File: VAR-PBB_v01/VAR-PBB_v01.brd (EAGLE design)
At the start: 78.4 x 86.4 mm, 20 parts, among them J1 ANDERSON_POWER_POLE, J11 CON1X2_SHROUDED, J2 ANDERSON_POWER_POLE, J3 CON1X2_SHROUDED, J4 CON1X2_SHROUDED, J5 CON1X2_SHROUDED, J6 CON1X2_SHROUDED, J7 CON1X2_SHROUDED, J8 CON1X2_SHROUDED, U1 OKI-78SR, U2 XL6009, U3 XL6009, U4 XL6009

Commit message: WIP, but got a ton done.
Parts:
- added C1, C4, C5: 0.1uF, SparkFun-Capacitors:0603
- added C2: 1.0uF, SparkFun-Capacitors:0603
- added C3: 2.2uF, SparkFun-Capacitors:0603
- added R1, R2, R3: (no value), SparkFun-Resistors:0603
- added U5: LP2985AIM5-1.5, LP2985AIM5-1.5:MF05A
- added U6: TPS259271DRCR, TPS259271DRCR:DRC10_1P65X2P40
- moved U$5 91.8 mm to (18.6, 80.0), flipped to the bottom
- moved J5 67.6 mm to (12.7, 33.0), turned to 0 degrees
- moved J3 67.5 mm to (12.7, 22.9), turned to 0 degrees
- moved J4 53.3 mm to (66.0, 73.7), turned to 180 degrees
- moved J8 53.3 mm to (66.0, 63.5), turned to 180 degrees
- moved U3 52.1 mm to (64.9, 35.0)
- moved U4 52.1 mm to (13.6, 34.9)
- moved J9 47.0 mm to (63.5, 2.54), turned to 180 degrees
- moved LOGO1 44.0 mm to (59.1, 82.4), flipped to the bottom
- moved J6 41.9 mm to (12.7, 63.5)
- moved J7 40.6 mm to (12.7, 73.7)
- moved J10 35.6 mm to (20.3, 2.54), turned to 180 degrees
- moved J11 1.80 mm to (66.0, 45.7)
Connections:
- removed net N$6: J10.1
- new net 1.5V_REG: C3.1, J10.1, U5.5
- new net N$12: R3.2, U6.10
- new net N$13: C5.2, U6.2
- new net N$14: R1.1, R2.2, U6.1
- new net N$8: C1.1, U5.4
- net BATT+: now also C2.1, C4.2, U5.1, U5.3, U6.6, U6.7, U6.8
- net GND: now also C1.2, C2.2, C3.2, C4.1, C5.1, R2.1, R3.1, U5.2, U6.11
- net N$1: now also R1.2, U6.3, U6.4, U6.5
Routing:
- net BATT+: track 0.00 -> 158.1 mm, vias 0 -> 3
- net CHANNEL4: track 0.00 -> 79.9 mm, vias 0 -> 1
- net CHANNEL3: track 0.00 -> 71.8 mm
- net 5V_REG: track 0.00 -> 69.8 mm
- net N$11: track 0.00 -> 40.8 mm
- net GND: track 0.00 -> 40.7 mm, vias 0 -> 4
- net N$1: track 0.00 -> 36.7 mm, vias 0 -> 2
- net N$7: track 0.00 -> 18.0 mm
- net N$5: track 0.00 -> 17.5 mm
- net 1.5V_REG: track 0.00 -> 12.6 mm
- net N$3: track 0.00 -> 12.2 mm
- net N$14: track 0.00 -> 4.78 mm
- net N$13: track 0.00 -> 3.99 mm
- net N$12: track 0.00 -> 2.71 mm
- net N$8: track 0.00 -> 2.39 mm
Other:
- board text added: "1.5V Output"
- board text added: "5V Output"
- board text added: "Fix"
- board text added: "Var"

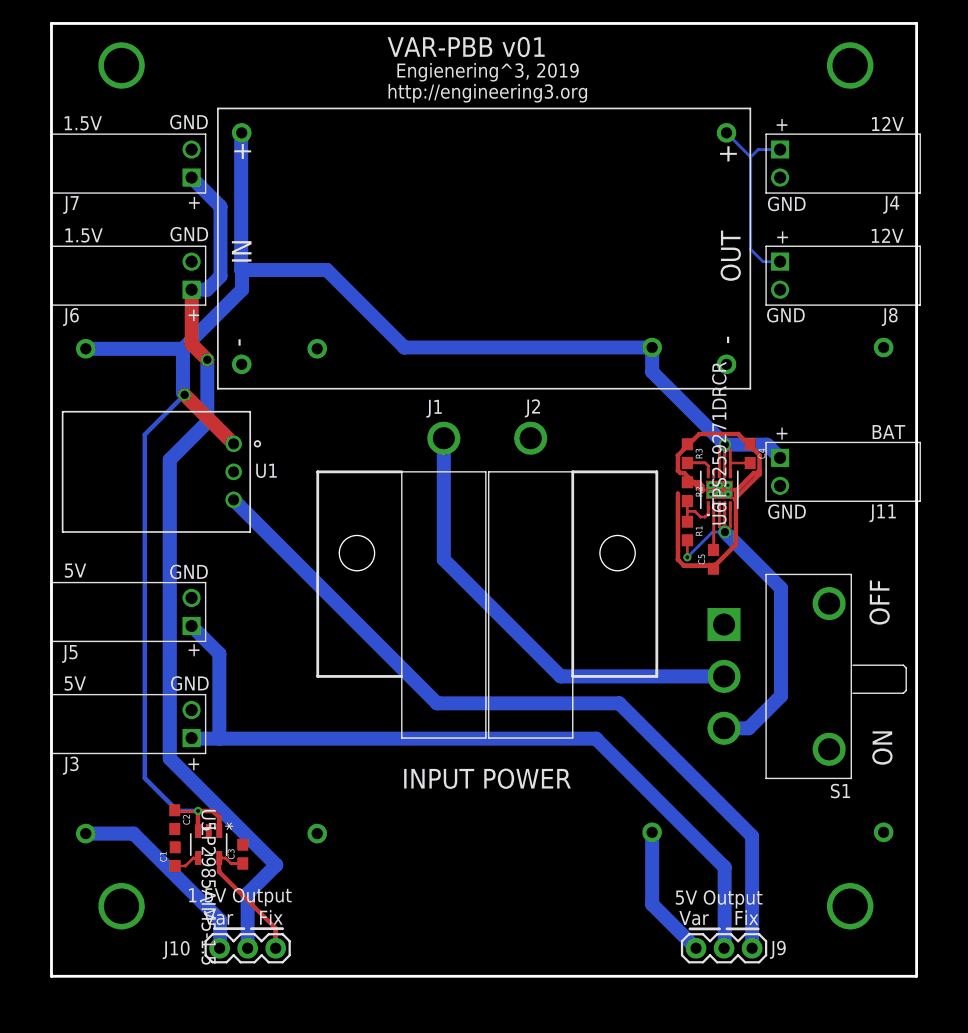
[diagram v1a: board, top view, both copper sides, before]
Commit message: Got all of the features in, board layout done, silk screen tweaked. Need to pick resistor values for UVLO and dV/dT, power LED, and finish BOM xls.
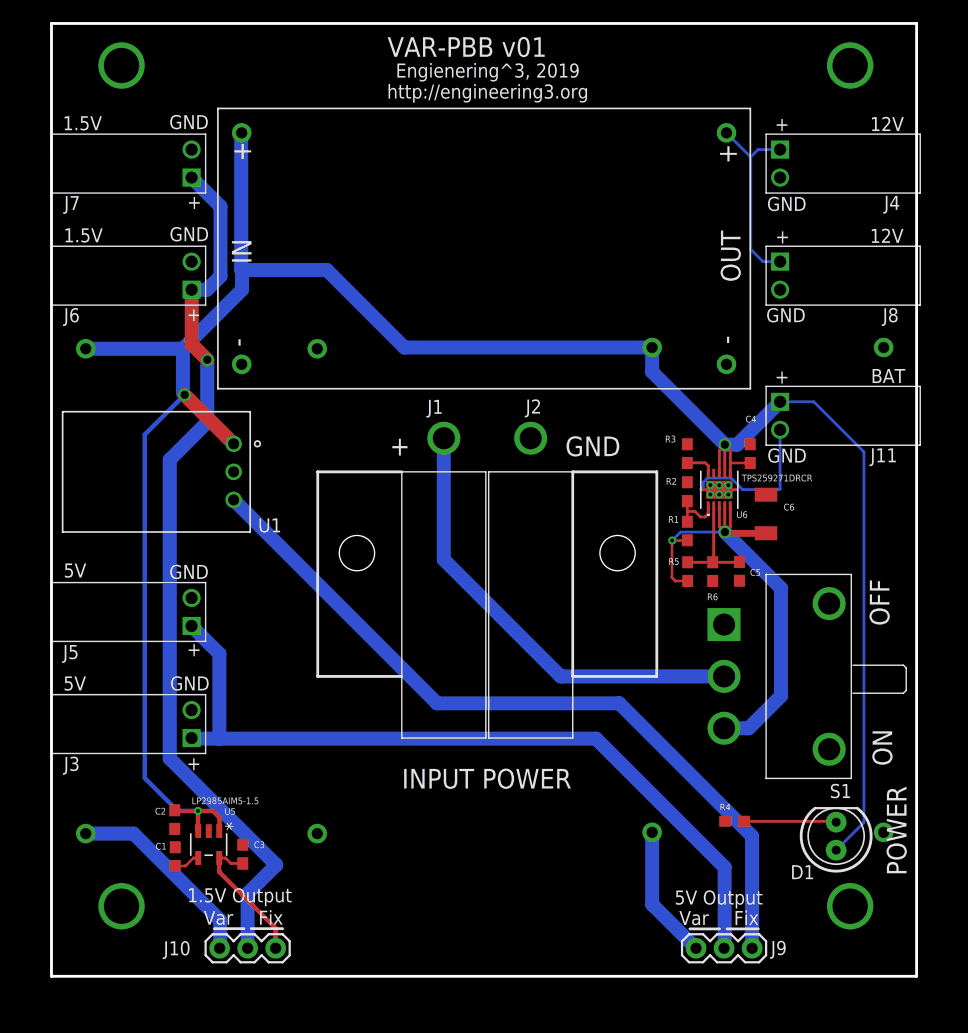
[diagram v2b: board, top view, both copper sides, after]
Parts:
- added C6: 22UF-1210-16V-20%, SparkFun-Capacitors:1210
- added D1: (no value), SparkFun-LED:LED_5MM
- added R4, R5, R6: (no value), SparkFun-Resistors:0603
- moved J11 5.08 mm to (66.0, 50.8)
- moved C5 2.60 mm to (62.4, 36.7)
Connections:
- removed net N$13: C5.2, U6.2
- new net N$2: D1.K, R4.2
- new net N$4: C5.2, R5.1, R6.2, U6.2
- net BATT+: now also D1.A
- net GND: now also C6.2, R4.1, R6.1
- net N$1: now also C6.1, R5.2
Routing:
- net BATT+: track 158.1 -> 205.8 mm
- net GND: track 40.7 -> 17.0 mm, vias 4 -> 10
- net N$4: track 0.00 -> 9.84 mm
- net N$1: track 36.7 -> 46.0 mm
- net N$2: track 0.00 -> 8.38 mm
- net N$13: track 3.99 -> 0.00 mm
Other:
- board text added: "POWER"

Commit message: v01 done - schematic complete and cleaned up, board fully routed, passes DRC, BOM complete.
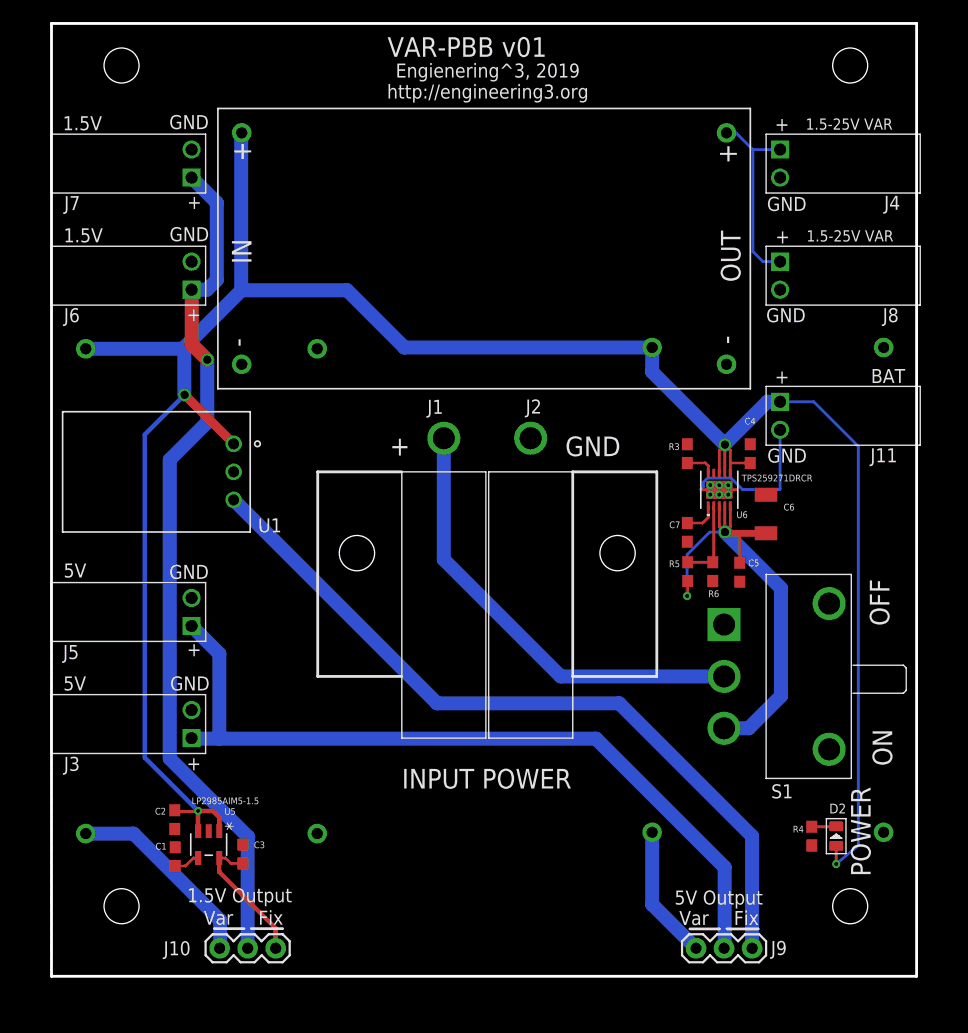
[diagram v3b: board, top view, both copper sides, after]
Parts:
- removed D1: (no value), SparkFun-LED:LED_5MM
- removed LOGO1: OSHW-LOGOM, SparkFun-Aesthetics:OSHW-LOGO-M
- removed R1, R2: (no value), SparkFun-Resistors:0603
- removed U$5: ROHS_GARBAGE, SchmalzHausPublic:ROHS_GARBAGE_5MM
- added C7: DNP, SparkFun-Capacitors:0603
- added D2: RED-0805, OPL_Optoelectronics:LED-0805
- C4, C5: value 0.1uF -> 1uF
- C6: value 22UF-1210-16V-20% -> 22uF
- R3: value (none) -> 45.3K
- R4: value (none) -> 392
- R5: value (none) -> 1M
- R6: value (none) -> 220K
- moved U$6 10.2 mm to (33.3, 3.43)
- moved LOGO2 8.98 mm to (25.7, 5.79)
- moved R4 7.11 mm to (68.9, 12.7), turned to 90 degrees
- moved C5 0.08 mm to (62.4, 36.6)
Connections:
- net BATT+: now also D2.+; no longer D1.A
- net GND: now also C7.1; no longer R2.1
- net N$1: now also C5.2; no longer R1.2
- net N$14: now also C7.2; no longer R1.1, R2.2
- net N$2: now also D2.-; no longer D1.K
- net N$4: no longer C5.2
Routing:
- net N$2: track 8.38 -> 2.23 mm
- net N$4: track 9.84 -> 7.41 mm
- net CHANNEL4: track 79.9 -> 77.5 mm
- net N$14: track 4.78 -> 3.13 mm
- net BATT+: track 205.8 -> 206.6 mm, vias 3 -> 4
- net N$1: track 46.0 -> 46.7 mm
- net GND: track 17.0 -> 16.8 mm, vias 10 -> 6
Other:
- board text added: "1.5-25V VAR"
- board text removed: "12V"

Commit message: Latest version of VAR-PBB, as built. Updated under voltage cutout resistor to get UVLO to around 8.1 V.
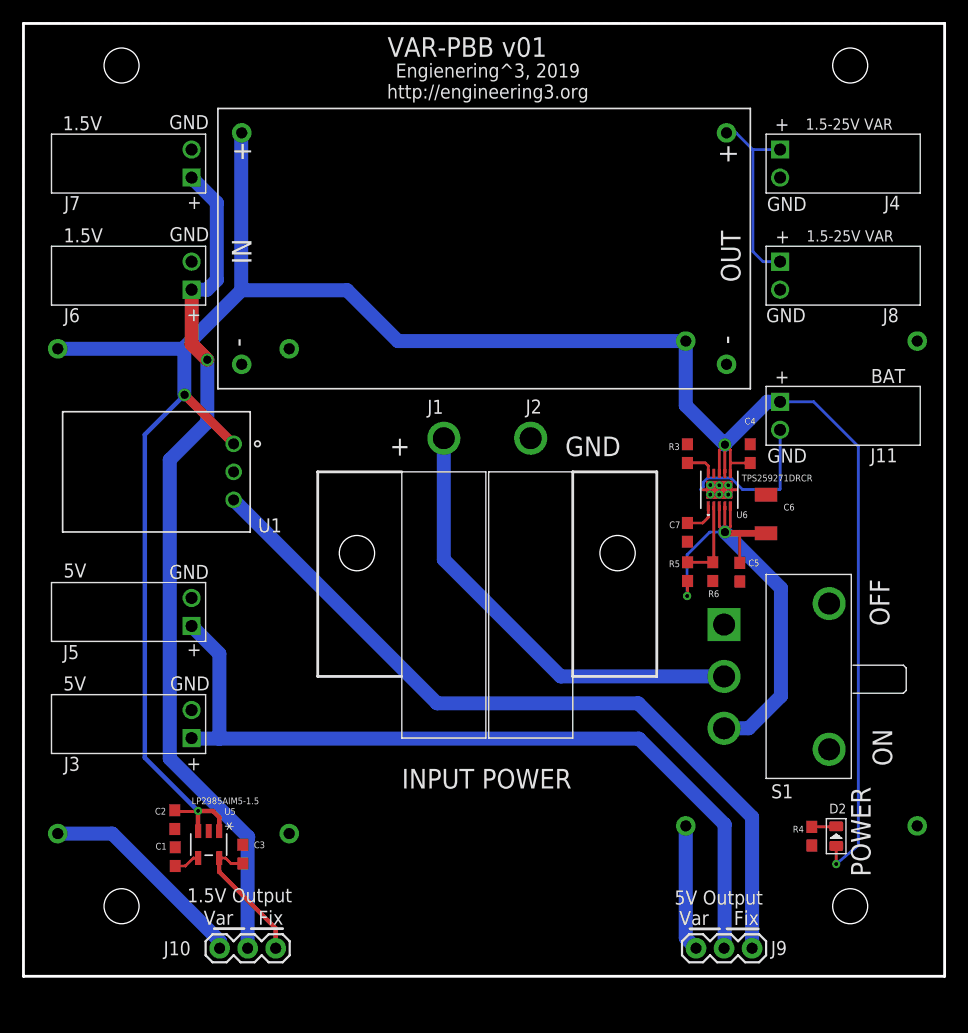
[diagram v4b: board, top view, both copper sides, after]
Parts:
- R6: value 220K -> 213K
- moved U3 3.10 mm to (68.0, 35.6)
- moved U4 2.54 mm to (11.1, 34.9)
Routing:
- net BATT+: track 206.6 -> 211.3 mm
- net CHANNEL3: track 71.8 -> 74.1 mm
- net N$7: track 18.0 -> 19.4 mm
- net 5V_REG: track 69.8 -> 70.8 mm
- net N$3: track 12.2 -> 11.5 mm
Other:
- board size 78.4 x 86.4 mm -> 83.5 x 86.4 mm
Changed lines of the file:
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@@
 <layer number="20" name="Dimension" color="15" fill="1" visible="yes" active="yes"/>
 <layer number="21" name="tPlace" color="7" fill="1" visible="yes" active="yes"/>
-<layer number="22" name="bPlace" color="7" fill="1" visible="no" active="yes"/>
-<layer number="23" name="tOrigins" color="15" fill="1" visible="no" active="yes"/>
-<layer number="24" name="bOrigins" color="15" fill="1" visible="no" active="yes"/>
+<layer number="22" name="bPlace" color="7" fill="1" visible="yes" active="yes"/>
+<layer number="23" name="tOrigins" color="15" fill="1" visible="yes" active="yes"/>
+<layer number="24" name="bOrigins" color="15" fill="1" visible="yes" active="yes"/>
 <layer number="25" name="tNames" color="7" fill="1" visible="no" active="yes"/>
 <layer number="26" name="bNames" color="7" fill="1" visible="no" active="yes"/>
@@
 <board>
 <plain>
-<wire x1="0" y1="0" x2="78.41" y2="0" width="0.254" layer="20"/>
-<wire x1="78.41" y1="0" x2="78.41" y2="86.36" width="0.254" layer="20"/>
-<wire x1="78.41" y1="86.36" x2="0" y2="86.36" width="0.254" layer="20"/>
-<wire x1="0" y1="86.36" x2="0" y2="0" width="0.254" layer="20"/>
+<wire x1="-2.54" y1="0" x2="80.95" y2="0" width="0.254" layer="20"/>
+<wire x1="80.95" y1="0" x2="80.95" y2="86.36" width="0.254" layer="20"/>
+<wire x1="80.95" y1="86.36" x2="-2.54" y2="86.36" width="0.254" layer="20"/>
+<wire x1="-2.54" y1="86.36" x2="-2.54" y2="0" width="0.254" layer="20"/>
 <wire x1="54.864" y1="45.72" x2="47.244" y2="45.72" width="0.254" layer="21"/>
 <wire x1="47.244" y1="45.72" x2="47.244" y2="27.178" width="0.254" layer="21"/>
@@
 </element>
 <element name="U2" library="XL6009_DC-DC" package="XL6009_MODULE" value="XL6009" x="39.2118" y="65.9554" smashed="yes" rot="R90"/>
-<element name="U3" library="XL6009_DC-DC" package="XL6009_MODULE" value="XL6009" x="64.9308" y="35.0186" smashed="yes" rot="MR0"/>
-<element name="U4" library="XL6009_DC-DC" package="XL6009_MODULE" value="XL6009" x="13.5974" y="34.9032" smashed="yes" rot="MR0"/>
+<element name="U3" library="XL6009_DC-DC" package="XL6009_MODULE" value="XL6009" x="67.9788" y="35.6028" smashed="yes" rot="MR0"/>
+<element name="U4" library="XL6009_DC-DC" package="XL6009_MODULE" value="XL6009" x="11.0574" y="34.9032" smashed="yes" rot="MR0"/>
 <element name="U1" library="OKI-78sr_Regulator" package="OKI-78SR_REGULATOR_HORIZONTAL" value="OKI-78SR" x="16.51" y="45.72" smashed="yes" rot="R90">
 <attribute name="NAME" x="18.7236" y="40.2374" size="1.27" layer="25" font="vector" ratio="18"/>
@@
 <attribute name="VALUE" x="56.4388" y="35.6108" size="0.6096" layer="27" font="vector" ratio="18" rot="R180" align="top-center"/>
 </element>
-<element name="R6" library="SparkFun-Resistors" library_urn="urn:adsk.eagle:library:532" package="0603" package3d_urn="urn:adsk.eagle:package:39650/1" value="220K" x="59.944" y="36.6776" smashed="yes" rot="R90">
+<element name="R6" library="SparkFun-Resistors" library_urn="urn:adsk.eagle:library:532" package="0603" package3d_urn="urn:adsk.eagle:package:39650/1" value="213K" x="59.944" y="36.6776" smashed="yes" rot="R90">
 <attribute name="NAME" x="60.0202" y="34.9758" size="0.6096" layer="25" font="vector" ratio="18" rot="R180" align="bottom-center"/>
 <attribute name="PROD_ID" value=" " x="59.944" y="36.6776" size="1.778" layer="27" rot="R90" display="off"/>
@@
 <contactref element="J7" pad="2"/>
 <polygon width="0.4064" layer="16" rank="2">
-<vertex x="-0.016115625" y="0"/>
-<vertex x="78.41" y="0"/>
-<vertex x="78.41" y="86.36"/>
-<vertex x="0" y="86.36"/>
+<vertex x="-2.556115625" y="0"/>
+<vertex x="80.95" y="0"/>
+<vertex x="80.95" y="86.36"/>
+<vertex x="-2.54" y="86.36"/>
 </polygon>
 <contactref element="J3" pad="2"/>
@@
 <contactref element="J8" pad="2"/>
 <polygon width="0.4064" layer="1">
-<vertex x="0" y="0"/>
-<vertex x="0" y="86.36"/>
-<vertex x="78.41" y="86.36"/>
-<vertex x="78.41" y="0"/>
+<vertex x="-2.54" y="0"/>
+<vertex x="-2.54" y="86.36"/>
+<vertex x="80.95" y="86.36"/>
+<vertex x="80.95" y="0"/>
 </polygon>
 <contactref element="U2" pad="IN-"/>
@@
 <wire x1="63.3222" y1="46.521" x2="61.54" y2="46.521" width="0.254" layer="1"/>
 <wire x1="61.54" y1="46.521" x2="61.5282" y2="46.5328" width="0.254" layer="1"/>
-<wire x1="61.0362" y1="48.1838" x2="54.4406" y2="54.7794" width="1.27" layer="16"/>
-<wire x1="54.4406" y1="54.7794" x2="54.4406" y2="56.9896" width="1.27" layer="16"/>
-<wire x1="54.4406" y1="56.9896" x2="31.9866" y2="56.9896" width="1.27" layer="16"/>
+<wire x1="61.0362" y1="48.1838" x2="57.4886" y2="51.7314" width="1.27" layer="16"/>
+<wire x1="57.4886" y1="51.7314" x2="57.4886" y2="57.5738" width="1.27" layer="16"/>
+<wire x1="57.4886" y1="57.5738" x2="31.4024" y2="57.5738" width="1.27" layer="16"/>
 <wire x1="26.797" y1="62.1792" x2="17.1958" y2="62.1792" width="1.27" layer="16"/>
 <wire x1="17.1958" y1="62.1792" x2="17.1958" y2="76.4006" width="1.27" layer="16"/>
 <wire x1="17.1958" y1="76.4006" x2="17.2408" y2="76.4456" width="0.254" layer="16"/>
-<wire x1="31.9866" y1="56.9896" x2="26.797" y2="62.1792" width="1.27" layer="16"/>
-<wire x1="3.1072" y1="56.8742" x2="11.9126" y2="56.8742" width="1.27" layer="16"/>
+<wire x1="31.4024" y1="57.5738" x2="26.797" y2="62.1792" width="1.27" layer="16"/>
+<wire x1="0.5672" y1="56.8742" x2="11.9126" y2="56.8742" width="1.27" layer="16"/>
 <wire x1="11.9126" y1="56.8742" x2="12.0396" y2="56.8742" width="1.27" layer="16"/>
 <wire x1="11.9126" y1="56.8742" x2="11.9162" y2="56.8742" width="0.254" layer="16"/>
@@
 <wire x1="12.7508" y1="21.5392" x2="15.2146" y2="21.5392" width="1.27" layer="16"/>
 <wire x1="12.7508" y1="21.5392" x2="12.7" y2="21.59" width="0.254" layer="16"/>
-<wire x1="15.2146" y1="21.5392" x2="49.3522" y2="21.5392" width="1.27" layer="16"/>
-<wire x1="49.3522" y1="21.5392" x2="61.0108" y2="9.8806" width="1.27" layer="16"/>
-<wire x1="61.0108" y1="9.8806" x2="61.0108" y2="2.5908" width="1.27" layer="16"/>
+<wire x1="15.2146" y1="21.5392" x2="53.2384" y2="21.5392" width="1.27" layer="16"/>
+<wire x1="53.2384" y1="21.5392" x2="61.0108" y2="13.7668" width="1.27" layer="16"/>
+<wire x1="61.0108" y1="13.7668" x2="61.0108" y2="2.5908" width="1.27" layer="16"/>
 <wire x1="61.0108" y1="2.5908" x2="60.96" y2="2.54" width="0.254" layer="16"/>
 </signal>
@@
 <contactref element="U3" pad="OUT+"/>
 <contactref element="J9" pad="3"/>
-<wire x1="54.4406" y1="13.0476" x2="54.4406" y2="6.5194" width="1.27" layer="16"/>
-<wire x1="54.4406" y1="6.5194" x2="58.42" y2="2.54" width="1.27" layer="16"/>
+<wire x1="57.4886" y1="13.6318" x2="57.4886" y2="3.4714" width="1.27" layer="16"/>
+<wire x1="57.4886" y1="3.4714" x2="58.42" y2="2.54" width="1.27" layer="16"/>
 </signal>
 <signal name="5V_REG">
@@
 <contactref element="U1" pad="P$3"/>
 <wire x1="16.51" y1="43.18" x2="34.9504" y2="24.7396" width="1.27" layer="16"/>
-<wire x1="51.4604" y1="24.7396" x2="63.5" y2="12.7" width="1.27" layer="16"/>
-<wire x1="63.5" y1="12.7" x2="63.5" y2="2.54" width="1.27" layer="16"/>
-<wire x1="34.9504" y1="24.7396" x2="51.4604" y2="24.7396" width="1.27" layer="16"/>
+<wire x1="53.1876" y1="24.7396" x2="63.5" y2="14.4272" width="1.27" layer="16"/>
+<wire x1="63.5" y1="14.4272" x2="63.5" y2="2.54" width="1.27" layer="16"/>
+<wire x1="34.9504" y1="24.7396" x2="53.1876" y2="24.7396" width="1.27" layer="16"/>
 </signal>
 <signal name="N$7">
 <contactref element="U4" pad="OUT+"/>
 <contactref element="J10" pad="3"/>
-<wire x1="3.1072" y1="12.9322" x2="7.4386" y2="12.9322" width="1.27" layer="16"/>
-<wire x1="7.4386" y1="12.9322" x2="15.2908" y2="5.08" width="1.27" layer="16"/>
-<wire x1="15.2908" y1="5.08" x2="15.2908" y2="2.5908" width="1.27" layer="16"/>
+<wire x1="0.5672" y1="12.9322" x2="5.5082" y2="12.9322" width="1.27" layer="16"/>
+<wire x1="5.5082" y1="12.9322" x2="15.2908" y2="3.1496" width="1.27" layer="16"/>
+<wire x1="15.2908" y1="3.1496" x2="15.2908" y2="2.5908" width="1.27" layer="16"/>
 <wire x1="15.2908" y1="2.5908" x2="15.24" y2="2.54" width="0.254" layer="16"/>
 </signal>
